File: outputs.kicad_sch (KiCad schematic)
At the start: 44 parts, among them J10 Bipolar/Inverted 2, J11 CV Out 2, J8 Bipolar/Inverted 1, J9 CV Out 1, U3 TL074, U4 TL074

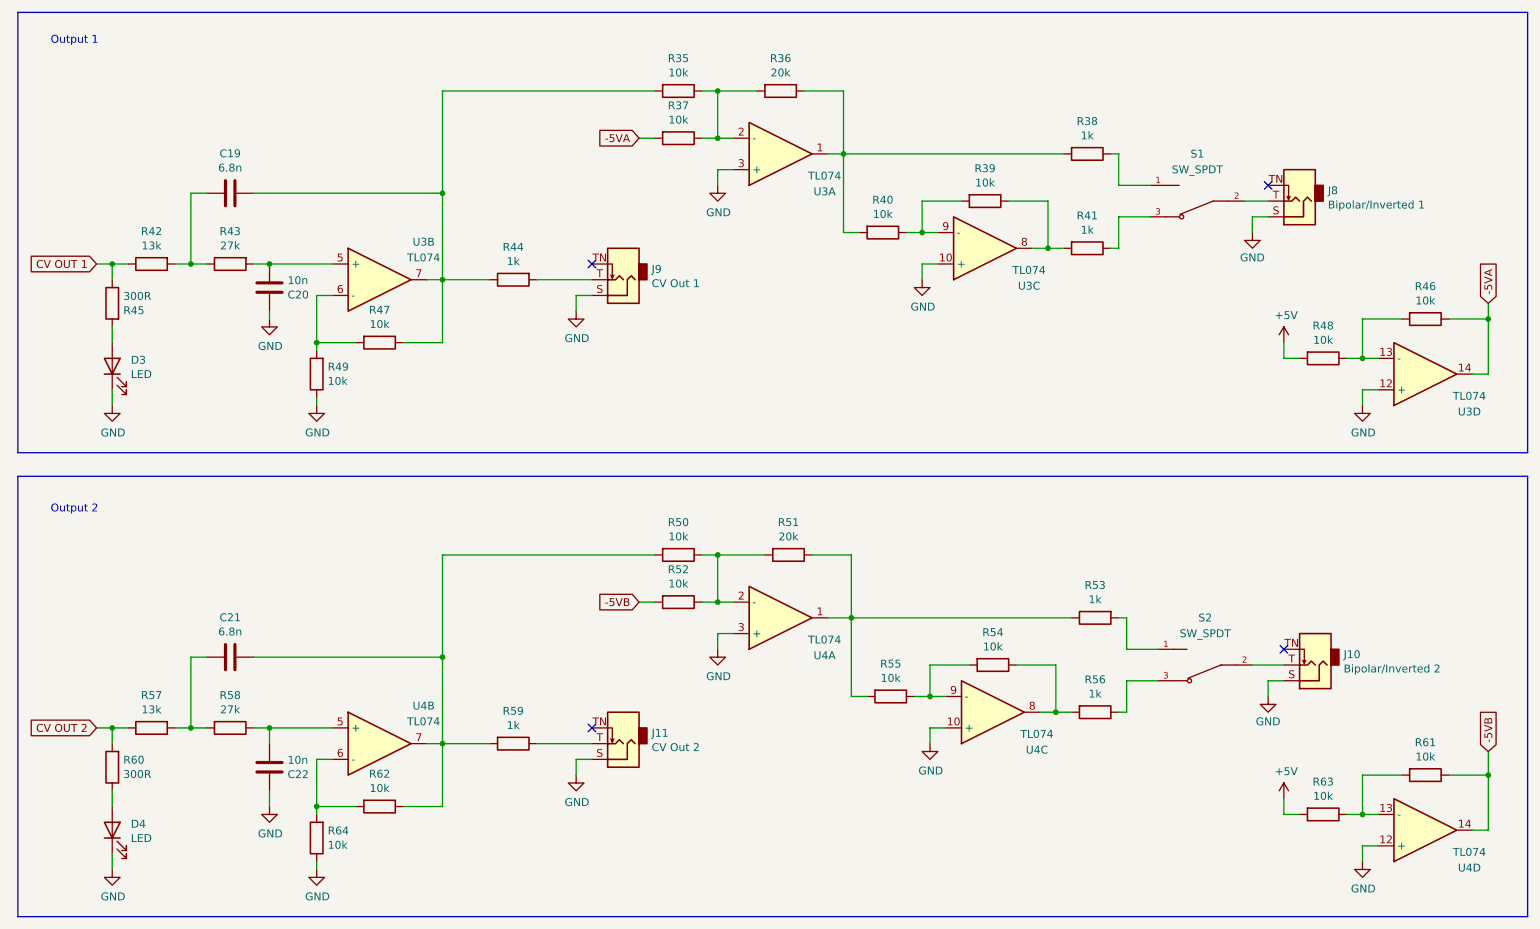
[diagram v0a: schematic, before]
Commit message: Reintroduce the DAC with gain boost from 4.096v to 9.99v. Refactor output LED, increase LED resistor value.
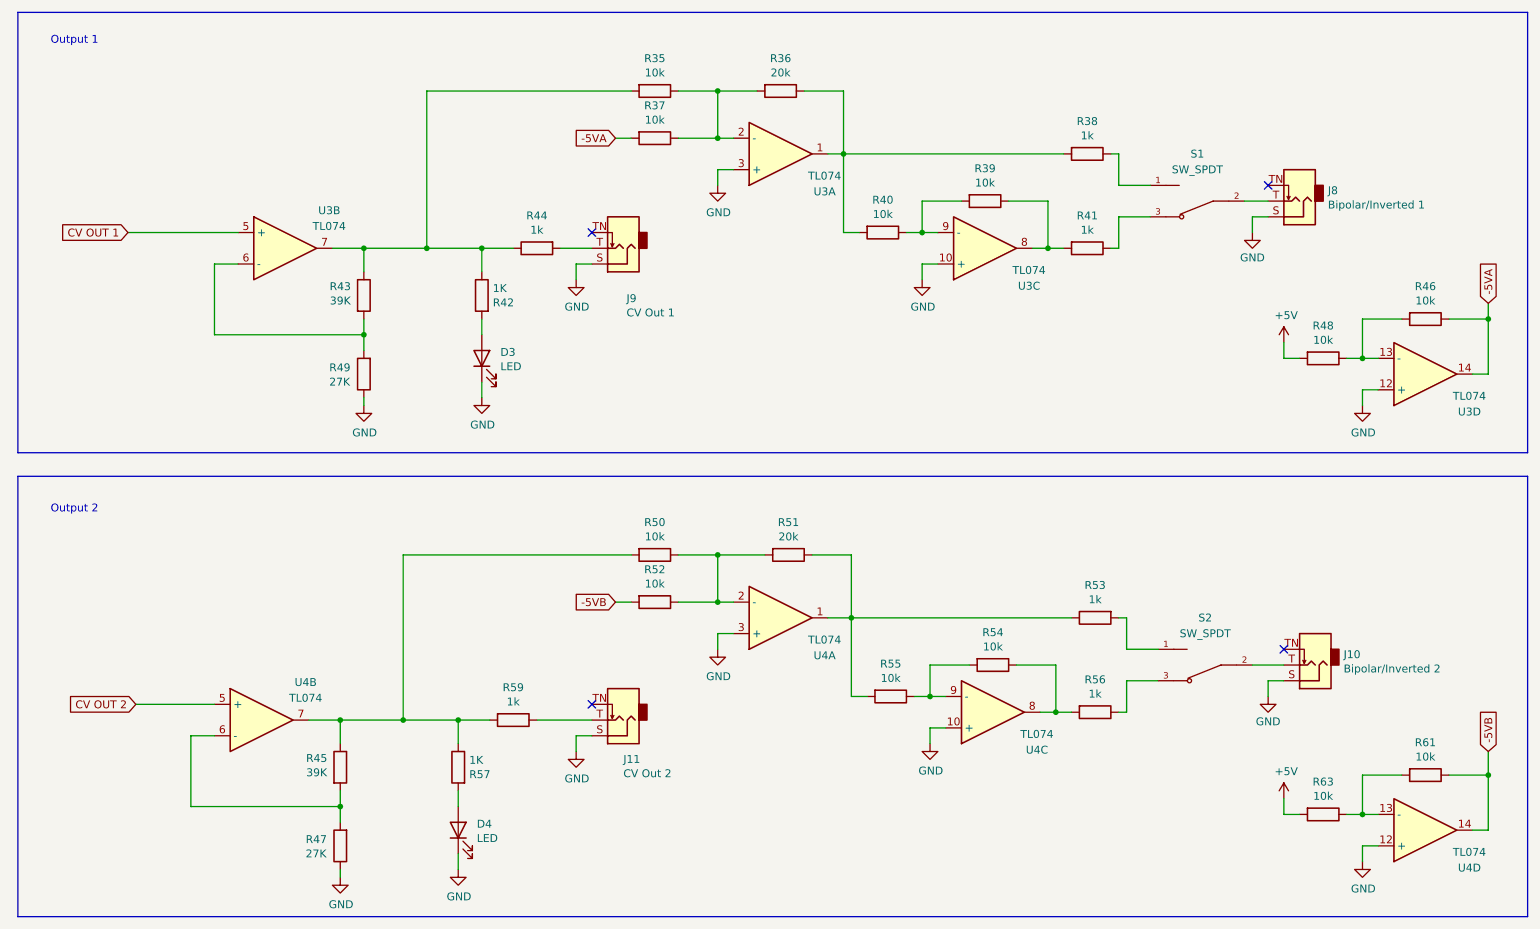
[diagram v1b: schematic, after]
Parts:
- removed C19, C21: 6.8n, Capacitor_SMD:C_0402_1005Metric, symbol Device:C
- removed C20, C22: 10n, Capacitor_SMD:C_0402_1005Metric, symbol Device:C
- removed R58: 27k, Resistor_SMD:R_0402_1005Metric, symbol Device:R
- removed R60: 300R, Resistor_SMD:R_0402_1005Metric, symbol Device:R
- removed R62, R64: 10k, Resistor_SMD:R_0402_1005Metric, symbol Device:R
- R42, R57: value 13k -> 1K; footprint Resistor_SMD:R_0603_1608Metric -> Resistor_SMD:R_0402_1005Metric; LCSC C22797 -> C11702
- R43: value 27k -> 39K; LCSC C25771 -> C25783
- R45: value 300R -> 39K; LCSC C25102 -> C25783
- R47, R49: value 10k -> 27K; LCSC C25744 -> C25771
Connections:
- net CV OUT 1: now also U3.5 (+); no longer R42.1, R45.1
- net CV OUT 2: now also U4.5 (+); no longer R57.1
- net GND: now also R47.1
- net at R35.2, R44.1, U3.7: now also R42.1, R43.1; no longer R47.1
- net at R49.2, U3.6 (-): now also R43.2; no longer R47.2
- net at D4.2 (A): now also R57.2
- net at R42.2: now also D3.2 (A); no longer R43.1
- net at R50.2, R59.2, U4.7: now also R45.1, R57.1
- net at U4.6 (-): now also R45.2, R47.2
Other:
- moved on the sheet: J11, J9, R35, R37, R44, R49, R50, R52, R59, U3B

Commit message: reorder annotations, replot pdf schematic
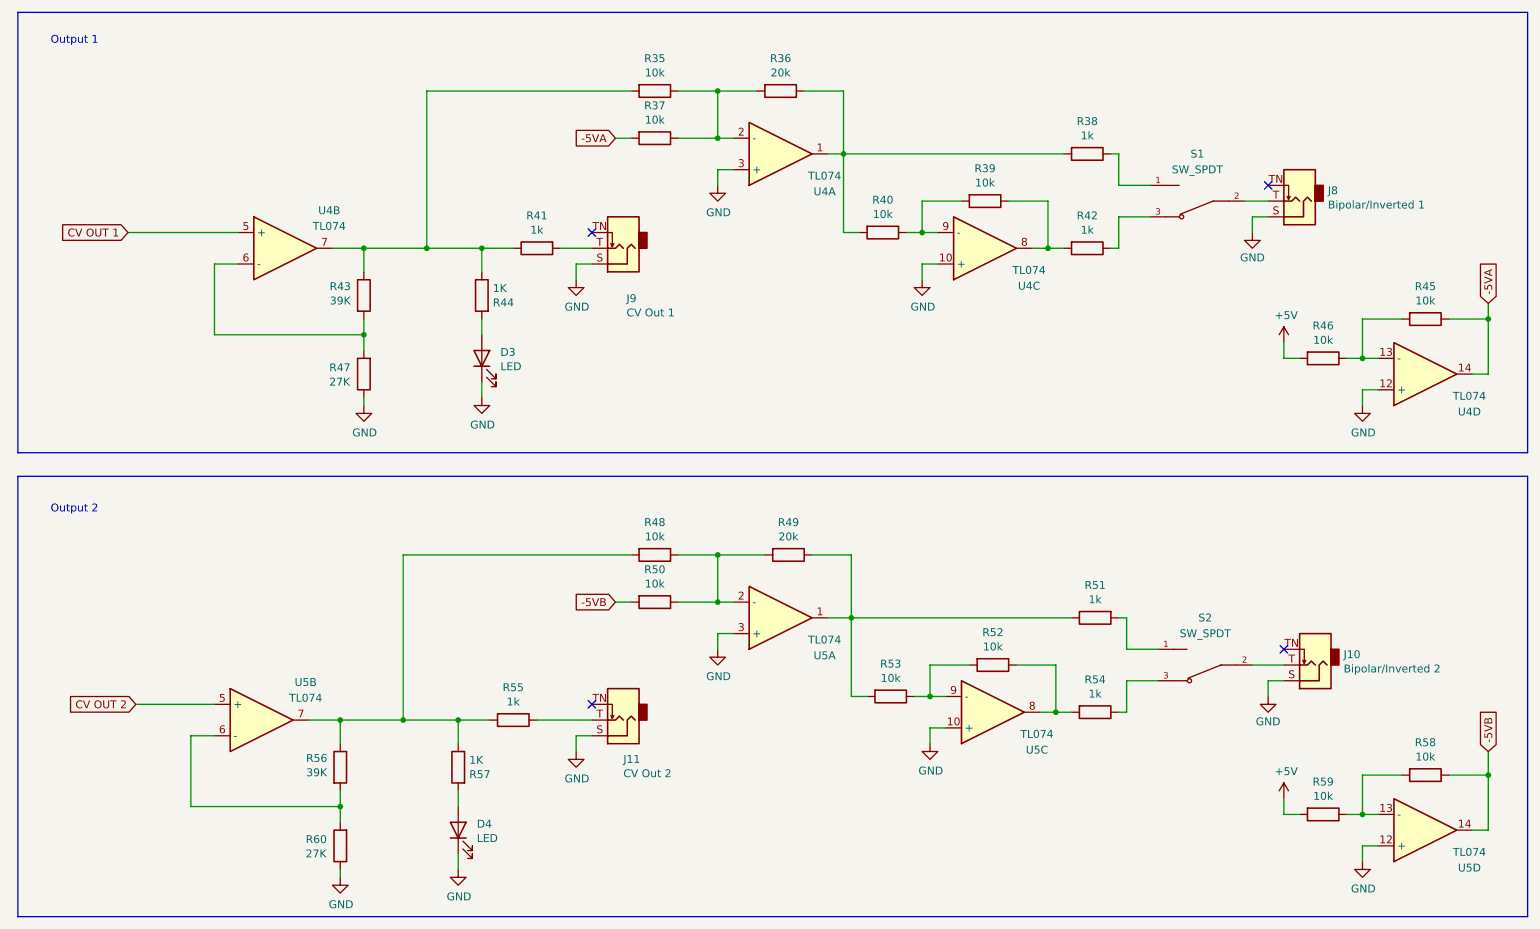
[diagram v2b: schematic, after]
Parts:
- renumbered R44 to R41, R41 to R42, R42 to R44, R46 to R45, R48 to R46, R49 to R47, R50 to R48, R51 to R49, R52 to R50, R53 to R51, R54 to R52, R55 to R53, R56 to R54, R59 to R55, R45 to R56, R61 to R58, R63 to R59, R47 to R60, U3 to U4, U4 to U5
